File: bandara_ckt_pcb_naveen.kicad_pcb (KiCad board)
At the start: 2 copper layers, 102.5 x 90 mm, 49 parts, among them J1 Nanopore, U1 MCP4725xxx-xCH, U2 ADS1115IDGS, U3 AD820, U4 Dual Power Supply, U5 AD820, U6 AD820

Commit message: fixed some PCB thing
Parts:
- added R14: 1M, Resistor_SMD:R_0603_1608Metric_Pad0.98x0.95mm_HandSolder, F.Cu at (126.0, 102.4)
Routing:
- net Net-(U6-Vout): track 12.2 -> 19.6 mm
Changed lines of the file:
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@@
 		)
 	)
+	(footprint "Resistor_SMD:R_0603_1608Metric_Pad0.98x0.95mm_HandSolder"
+		(layer "F.Cu")
+		(at 126 102.4125 -90)
+		(descr "Resistor SMD 0603 (1608 Metric), square (rectangular) end terminal, IPC_7351 nominal with elongated pad for handsoldering. (Body size source: IPC-SM-782 page 72, https://www.pcb-3d.com/wordpress/wp-content/uploads/ipc-sm-782a_amendment_1_and_2.pdf), generated with kicad-footprint-generator")
+		(tags "resistor handsolder")
+		(property "Reference" "R14"
+			(at 0 -1.43 90)
+			(layer "F.SilkS")
+			(effects
+				(font
+					(size 1 1)
+					(thickness 0.15)
+				)
+			)
+		)
+		(property "Value" "1M"
+			(at 0 1.43 90)
+			(layer "F.Fab")
+			(effects
+				(font
+					(size 1 1)
+					(thickness 0.15)
+				)
+			)
+		)
+		(property "Footprint" "Resistor_SMD:R_0603_1608Metric_Pad0.98x0.95mm_HandSolder"
+			(at 0 0 -90)
+			(unlocked yes)
+			(layer "F.Fab")
+			(hide yes)
+			(effects
+				(font
+					(size 1.27 1.27)
+					(thickness 0.15)
+				)
+			)
+		)
+		(property "Datasheet" ""
+			(at 0 0 -90)
+			(unlocked yes)
+			(layer "F.Fab")
+			(hide yes)
+			(effects
+				(font
+					(size 1.27 1.27)
+					(thickness 0.15)
+				)
+			)
+		)
+		(property "Description" "Resistor"
+			(at 0 0 -90)
+			(unlocked yes)
+			(layer "F.Fab")
+			(hide yes)
+			(effects
+				(font
+					(size 1.27 1.27)
+					(thickness 0.15)
+				)
+			)
+		)
+		(property ki_fp_filters "R_*")
+		(sheetname "Root")
+		(sheetfile "bandara_ckt_pcb_naveen.kicad_sch")
+		(attr smd)
+		(fp_line
+			(start -0.254724 0.5225)
+			(end 0.254724 0.5225)
+			(stroke
+				(width 0.12)
+				(type solid)
+			)
+			(layer "F.SilkS")
+		)
+		(fp_line
+			(start -0.254724 -0.5225)
+			(end 0.254724 -0.5225)
+			(stroke
+				(width 0.12)
+				(type solid)
+			)
+			(layer "F.SilkS")
+		)
+		(fp_line
+			(start -1.65 0.73)
+			(end -1.65 -0.73)
+			(stroke
+				(width 0.05)
+				(type solid)
+			)
+			(layer "F.CrtYd")
+		)
+		(fp_line
+			(start 1.65 0.73)
+			(end -1.65 0.73)
+			(stroke
+				(width 0.05)
+				(type solid)
+			)
+			(layer "F.CrtYd")
+		)
+		(fp_line
+			(start -1.65 -0.73)
+			(end 1.65 -0.73)
+			(stroke
+				(width 0.05)
+				(type solid)
+			)
+			(layer "F.CrtYd")
+		)
+		(fp_line
+			(start 1.65 -0.73)
+			(end 1.65 0.73)
+			(stroke
+				(width 0.05)
+				(type solid)
+			)
+			(layer "F.CrtYd")
+		)
+		(fp_line
+			(start -0.8 0.4125)
+			(end -0.8 -0.4125)
+			(stroke
+				(width 0.1)
+				(type solid)
+			)
+			(layer "F.Fab")
+		)
+		(fp_line
+			(start 0.8 0.4125)
+			(end -0.8 0.4125)
+			(stroke
+				(width 0.1)
+				(type solid)
+			)
+			(layer "F.Fab")
+		)
+		(fp_line
+			(start -0.8 -0.4125)
+			(end 0.8 -0.4125)
+			(stroke
+				(width 0.1)
+				(type solid)
+			)
+			(layer "F.Fab")
+		)
+		(fp_line
+			(start 0.8 -0.4125)
+			(end 0.8 0.4125)
+			(stroke
+				(width 0.1)
+				(type solid)
+			)
+			(layer "F.Fab")
+		)
+		(fp_text user "${REFERENCE}"
+			(at 0 0 90)
+			(layer "F.Fab")
+			(effects
+				(font
+					(size 0.4 0.4)
+					(thickness 0.06)
+				)
+			)
+		)
+		(pad "1" smd roundrect
+			(at -0.9125 0 270)
+			(size 0.975 0.95)
+			(layers "F.Cu" "F.Paste" "F.Mask")
+			(roundrect_rratio 0.25)
+			(net 39 "Net-(U6--IN)")
+			(pintype "passive")
+		)
+		(pad "2" smd roundrect
+			(at 0.9125 0 270)
+			(size 0.975 0.95)
+			(layers "F.Cu" "F.Paste" "F.Mask")
+			(roundrect_rratio 0.25)
+			(net 42 "Net-(U6-Vout)")
+			(pintype "passive")
+		)
+		(model "${KICAD8_3DMODEL_DIR}/Resistor_SMD.3dshapes/R_0603_1608Metric.wrl"
+			(offset
+				(xyz 0 0 0)
+			)
+			(scale
+				(xyz 1 1 1)
+			)
+			(rotate
+				(xyz 0 0 0)
+			)
+		)
+	)
 	(footprint "Capacitor_THT:C_Radial_D8.0mm_H11.5mm_P3.50mm"
 		(layer "F.Cu")
@@
 		(net 42)
 	)
+	(segment
+		(start 130.65 103.5)
+		(end 126.5 103.5)
+		(width 0.2)
+		(layer "B.Cu")
+		(net 42)
+	)
+	(segment
+		(start 132.96 105.81)
+		(end 130.65 103.5)
+		(width 0.2)
+		(layer "B.Cu")
+		(net 42)
+	)

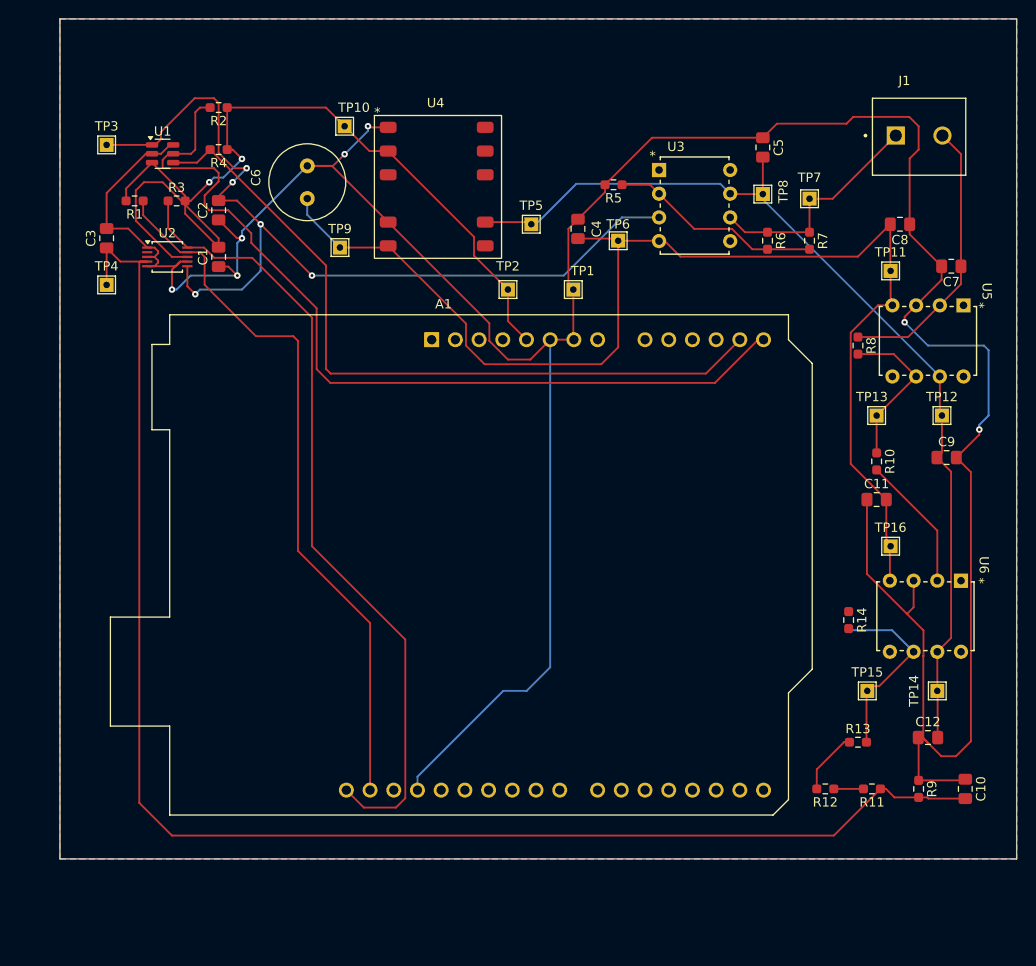
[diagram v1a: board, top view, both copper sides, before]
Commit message: The Required correction is done
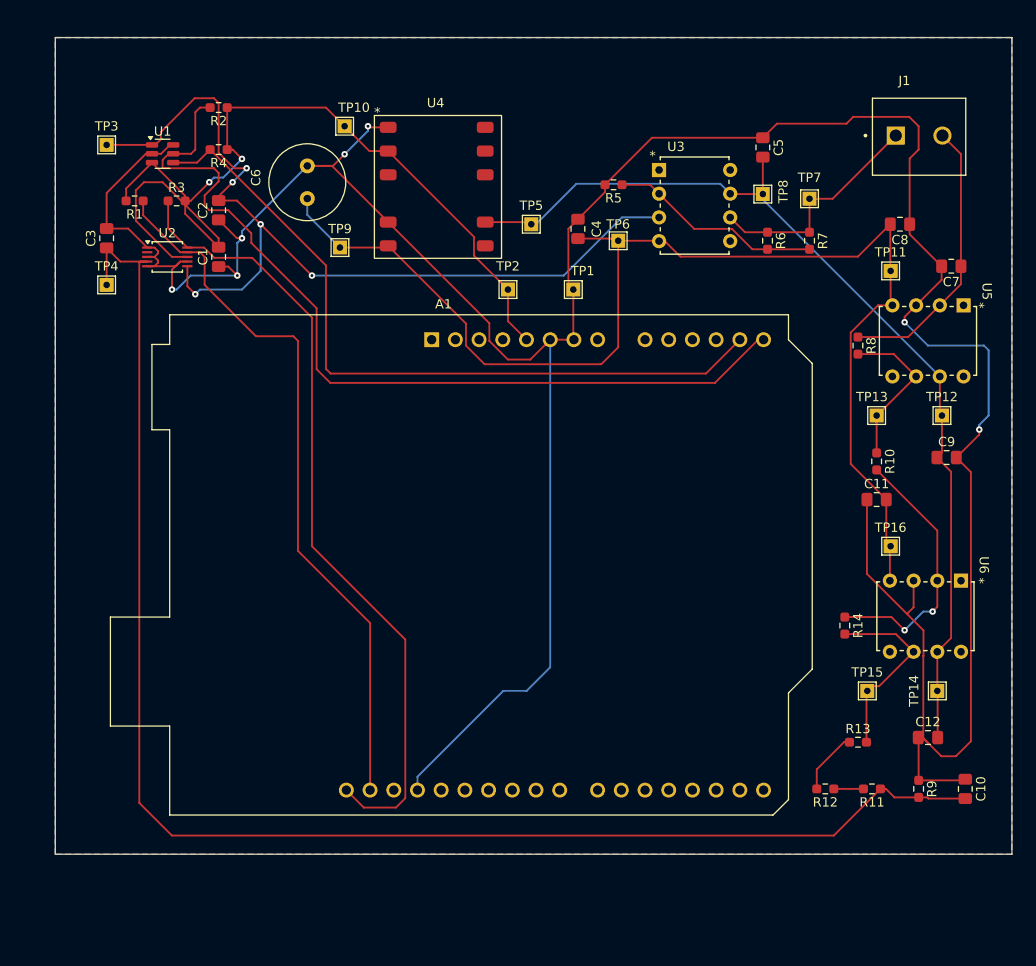
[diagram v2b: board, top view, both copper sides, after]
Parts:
- moved R14 0.72 mm to (125.6, 103.0)
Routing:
- net Net-(U6--IN): track 14.6 -> 28.9 mm, vias 0 -> 2
- net Net-(U6-Vout): track 19.6 -> 20.4 mm
- added copper zone on B.Cu, net +5V
- added copper zone on F.Cu, net +5V
- removed copper zone on B.Cu, net +VSW
- removed copper zone on F.Cu, net +VSW
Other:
- board size 102.5 x 90 mm -> 102.5 x 87.5 mm

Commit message: PCB and Schematic updated after YES from Bandara
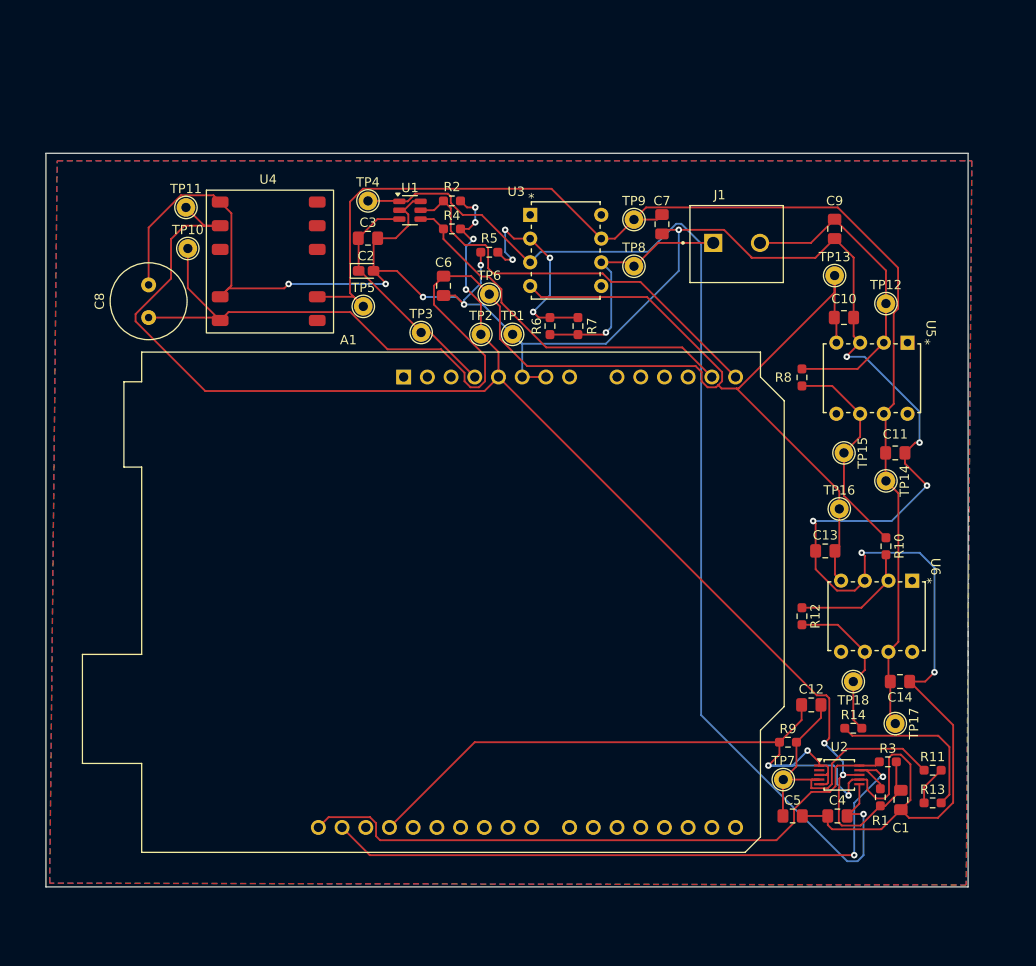
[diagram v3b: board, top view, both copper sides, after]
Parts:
- added C13: 100n, Capacitor_SMD:C_0805_2012Metric_Pad1.18x1.45mm_HandSolder, F.Cu at (123.5, 95.0)
- added C14: 100n, Capacitor_SMD:C_0805_2012Metric_Pad1.18x1.45mm_HandSolder, F.Cu at (131.5, 109.0)
- added TP17: TestPoint, TestPoint:TestPoint_THTPad_D2.0mm_Drill1.0mm, F.Cu at (131.0, 113.5)
- added TP18: TestPoint, TestPoint:TestPoint_THTPad_D2.0mm_Drill1.0mm, F.Cu at (126.5, 109.0)
- C2: value 100n -> 10u; footprint Capacitor_SMD:C_0805_2012Metric_Pad1.18x1.45mm_HandSolder -> Capacitor_Tantalum_SMD:CP_EIA-1608-08_AVX-J_Pad1.25x1.05mm_HandSolder
- C6: value 47u -> 100n; footprint Capacitor_THT:C_Radial_D8.0mm_H11.5mm_P3.50mm -> Capacitor_SMD:C_0805_2012Metric_Pad1.18x1.45mm_HandSolder
- C8: value 100n -> 47u; footprint Capacitor_SMD:C_0805_2012Metric_Pad1.18x1.45mm_HandSolder -> Capacitor_THT:C_Radial_D8.0mm_H11.5mm_P3.50mm
- TP1, TP10, TP11, TP12, TP13, TP14, TP15, TP16, TP2, TP3, TP4, TP5, TP6, TP7, TP8, TP9: footprint TestPoint:TestPoint_THTPad_1.5x1.5mm_Drill0.7mm -> TestPoint:TestPoint_THTPad_D2.0mm_Drill1.0mm
- moved R1 102.3 mm to (129.4, 121.4), turned to -90 degrees
- moved R3 97.0 mm to (130.2, 117.6)
- moved C1 93.4 mm to (131.6, 121.7)
- moved U2 90.9 mm to (125.0, 119.0)
- moved C8 81.1 mm to (51.0, 70.0), turned to 90 degrees
- moved TP11 75.8 mm to (55.0, 58.2)
- moved C5 71.7 mm to (120.0, 123.4), turned to 0 degrees
- moved C4 68.8 mm to (124.8, 123.4), turned to 0 degrees
- moved TP7 62.3 mm to (119.0, 119.5)
- moved C10 52.1 mm to (125.5, 70.0), turned to 180 degrees
- moved TP3 39.2 mm to (80.2, 71.6)
- moved TP9 31.6 mm to (103.0, 59.5)
- moved C7 31.3 mm to (106.0, 60.0), turned to 90 degrees
- moved TP4 29.4 mm to (74.5, 57.5)
- moved C3 28.0 mm to (74.5, 61.5), turned to 0 degrees
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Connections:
- A1 pad 4: unconnected-(A1-3V3-Pad4) -> +3.3V
- C10 pad 2: Net-(U2-AIN0) -> -VSW
- C11 pad 1: GND -> +VSW
- C11 pad 2: -VSW -> GND
- C12 pad 2: +VSW -> Net-(U2-AIN0)
- C2 pad 1: GND -> +3.3V
- C2 pad 2: Net-(U1-VOUT) -> GND
- C3 pad 1: Net-(U2-AIN0) -> +3.3V
- C4 pad 2: -VSW -> Net-(U1-VOUT)
- C5 pad 1: GND -> Net-(U2-AIN0)
- C5 pad 2: +VSW -> GND
- C6 pad 1: -VSW -> GND
- C6 pad 2: GND -> -VSW
- C7 pad 1: Net-(J1-Pin_2) -> GND
- C7 pad 2: GND -> +VSW
- C8 pad 1: GND -> -VSW
- C8 pad 2: -VSW -> GND
- C9 pad 1: +VSW -> Net-(J1-Pin_2)
- R12 pad 1: Net-(R11-Pad2) -> Net-(U6--IN)
- R12 pad 2: Net-(R12-Pad2) -> Net-(U6-Vout)
- R13 pad 1: Net-(R12-Pad2) -> Net-(R11-Pad2)
- R13 pad 2: Net-(U6-Vout) -> Net-(R13-Pad2)
- R14 pad 1: Net-(U6--IN) -> Net-(R13-Pad2)
- TP10 pad 1: +5V -> -VSW
- TP11 pad 1: -VSW -> +5V
- TP12 pad 1: +VSW -> Net-(J1-Pin_2)
- TP13 pad 1: Net-(U5-Vout) -> -VSW
- TP15 pad 1: Net-(U6-Vout) -> Net-(U5-Vout)
- TP3 pad 1: Net-(U1-VOUT) -> +3.3V
- TP4 pad 1: Net-(U2-AIN0) -> Net-(U1-VOUT)
- TP7 pad 1: Net-(J1-Pin_1) -> Net-(U2-AIN0)
- TP8 pad 1: +VSW -> Net-(J1-Pin_1)
- TP9 pad 1: -VSW -> +VSW
- U1 pad 3: +5V -> +3.3V
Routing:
- net Net-(U2-AIN0): track 160.2 -> 35.2 mm
- net +5V: track 100.3 -> 164.8 mm, vias 2 -> 6
- net Net-(U1-SCL): track 95.1 -> 44.7 mm
- net -VSW: track 133.9 -> 178.5 mm
- net Net-(U1-SDA): track 79.2 -> 39.7 mm
- net +VSW: track 103.7 -> 136.8 mm
- net Net-(U1-VOUT): track 98.0 -> 127.0 mm, vias 5 -> 1
- net +3.3V: track 0.00 -> 26.0 mm
- net Net-(R13-Pad2): track 0.00 -> 18.4 mm
- net Net-(U2-SCL): track 85.5 -> 67.9 mm
- net Net-(U6--IN): track 28.9 -> 13.4 mm, vias 2 -> 0
- net GND: track 348.3 -> 355.5 mm, vias 7 -> 15
- net Net-(R12-Pad2): track 6.79 -> 0.00 mm
- net Net-(U5-Vout): track 18.2 -> 23.3 mm
- net Net-(U2-SDA): track 76.8 -> 72.1 mm, vias 0 -> 2
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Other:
- board size 102.5 x 87.5 mm -> 98.8 x 78.6 mm

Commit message: Changes
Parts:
- moved R10 93.9 mm to (46.2, 136.9), turned to 0 degrees
- moved R8 93.1 mm to (46.2, 131.8), turned to 0 degrees
- moved U5 91.1 mm to (52.1, 115.8), turned to 0 degrees
- moved R3 89.4 mm to (41.9, 131.8)
- moved R1 87.7 mm to (41.9, 126.8), turned to 0 degrees
- moved J1 87.6 mm to (54.2, 134.6)
- moved R5 86.8 mm to (41.9, 136.9), turned to 0 degrees
- moved TP12 85.1 mm to (78.2, 136.0)
- moved R13 85.0 mm to (50.6, 131.8)
- moved R11 84.8 mm to (50.6, 126.8)
- moved R4 84.8 mm to (41.9, 134.3), turned to 0 degrees
- moved R2 83.0 mm to (41.9, 129.3), turned to 0 degrees
- moved U1 81.0 mm to (111.1, 132.8)
- moved C2 80.2 mm to (110.8, 136.4)
- moved C8 79.2 mm to (102.0, 130.6), turned to 0 degrees
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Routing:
- net GND: track 355.5 -> 0.00 mm, vias 15 -> 0
- net -VSW: track 178.5 -> 0.00 mm
- net +5V: track 164.8 -> 0.00 mm, vias 6 -> 0
- net +VSW: track 136.8 -> 0.00 mm
- net Net-(U1-VOUT): track 127.0 -> 0.00 mm, vias 1 -> 0
- net Net-(U2-SDA): track 72.1 -> 0.00 mm, vias 2 -> 0
- net Net-(U2-SCL): track 67.9 -> 0.00 mm
- net Net-(U1-SCL): track 44.7 -> 0.00 mm
- net Net-(U1-SDA): track 39.7 -> 0.00 mm
- net Net-(U2-AIN0): track 35.2 -> 0.00 mm
- net Net-(J1-Pin_2): track 34.6 -> 0.00 mm
- net Net-(J1-Pin_1): track 27.5 -> 0.00 mm, vias 1 -> 0
- net +3.3V: track 26.0 -> 0.00 mm
- net Net-(U5-Vout): track 23.3 -> 0.00 mm
- net Net-(U3--IN): track 23.1 -> 0.00 mm, vias 4 -> 0
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- removed copper zone on B.Cu, net +5V
- removed copper zone on F.Cu, net +5V
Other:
- board outline removed

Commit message: Final before check
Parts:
- moved J1 100.9 mm to (115.7, 54.5)
- moved R5 100.5 mm to (88.6, 47.9), turned to 180 degrees
- moved R10 95.8 mm to (126.9, 85.1), turned to -90 degrees
- moved R8 95.6 mm to (118.6, 69.3), turned to -90 degrees
- moved R7 95.3 mm to (102.7, 52.6), turned to -90 degrees
- moved R4 95.1 mm to (72.2, 44.2)
- moved R6 95.0 mm to (105.6, 52.6), turned to -90 degrees
- moved U5 93.0 mm to (130.1, 65.1), turned to -90 degrees
- moved C2 92.7 mm to (83.1, 47.9)
- moved C8 92.5 mm to (48.6, 55.0), turned to 90 degrees
- moved U1 91.8 mm to (78.0, 47.2), turned to 180 degrees
- moved TP12 91.8 mm to (127.3, 58.5)
- moved TP11 89.6 mm to (51.9, 46.3)
- moved R2 87.6 mm to (72.2, 47.1)
- moved U3 86.2 mm to (92.4, 46.4)
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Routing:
- net GND: track 0.00 -> 386.6 mm, vias 0 -> 6
- net +5V: track 0.00 -> 239.3 mm, vias 0 -> 2
- net -VSW: track 0.00 -> 122.1 mm
- net +VSW: track 0.00 -> 110.1 mm, vias 0 -> 1
- net Net-(U1-VOUT): track 0.00 -> 101.8 mm, vias 0 -> 1
- net Net-(U2-SCL): track 0.00 -> 73.0 mm
- net Net-(U2-SDA): track 0.00 -> 70.7 mm
- net Net-(U1-SDA): track 0.00 -> 67.4 mm
- net Net-(U3--IN): track 0.00 -> 48.1 mm, vias 0 -> 1
- net Net-(U1-SCL): track 0.00 -> 45.9 mm, vias 0 -> 1
- net +3.3V: track 0.00 -> 35.7 mm, vias 0 -> 1
- net Net-(J1-Pin_2): track 0.00 -> 27.0 mm
- net Net-(U2-AIN0): track 0.00 -> 23.5 mm
- net Net-(U5-Vout): track 0.00 -> 19.7 mm
- net Net-(J1-Pin_1): track 0.00 -> 19.0 mm
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- added copper zone on F.Cu, net +VSW
- added copper zone on B.Cu, net -VSW
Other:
- board outline added: 98.8 x 81.1 mm
